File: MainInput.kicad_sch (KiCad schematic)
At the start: 26 parts, among them J14 PJ-082BH, J15 DB9_Female_RA, J33 Conn_01x04_Female, U9 MAX3232

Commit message: First try to fit electronic on PCB
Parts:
- removed TP255, TP256, TP257, TP258, TP259, TP260: TestPoint_Small, Connector_PinHeader_2.54mm:PinHeader_1x01_P2.54mm_Vertical, symbol Connector:TestPoint_Small
- TP92: renamed from TP182; footprint Connector_PinHeader_2.54mm:PinHeader_1x01_P2.54mm_Vertical -> Connector_Pin:Pin_D1.0mm_L10.0mm
- TP94: renamed from TP183; footprint Connector_Pin:Pin_D1.2mm_L11.3mm_W3.0mm_Flat -> Connector_Pin:Pin_D1.0mm_L10.0mm
- TP97: renamed from TP185; footprint Connector_Pin:Pin_D1.2mm_L11.3mm_W3.0mm_Flat -> Connector_Pin:Pin_D1.0mm_L10.0mm
- TP98: renamed from TP186; footprint Connector_Pin:Pin_D1.2mm_L11.3mm_W3.0mm_Flat -> Connector_Pin:Pin_D1.0mm_L10.0mm
- renumbered D48 to D34, D49 to D35, J14 to J27, J15 to J28, J33 to J29, NT456 to NT468, NT457 to NT469, R81 to R68

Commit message: backup 1 bank done
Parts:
- NT468, NT469: footprint NetTie:NetTie-2_THT_Pad1.0mm -> NetTie:NetTie-2_Front1.0mm
- TP92, TP94, TP97, TP98: footprint Connector_Pin:Pin_D1.0mm_L10.0mm -> Connector_Pin:Pin_D0.9mm_L10.0mm_W2.4mm_FlatFork
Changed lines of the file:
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@@
       (effects (font (size 1.27 1.27)) (justify left))
     )
-    (property "Footprint" "Connector_Pin:Pin_D1.0mm_L10.0mm" (id 2) (at 105.41 107.95 0)
+    (property "Footprint" "Connector_Pin:Pin_D0.9mm_L10.0mm_W2.4mm_FlatFork" (id 2) (at 105.41 107.95 0)
       (effects (font (size 1.27 1.27)) hide)
     )
@@
       (effects (font (size 1.27 1.27)) (justify left))
     )
-    (property "Footprint" "Connector_Pin:Pin_D1.0mm_L10.0mm" (id 2) (at 63.5 102.87 0)
+    (property "Footprint" "Connector_Pin:Pin_D0.9mm_L10.0mm_W2.4mm_FlatFork" (id 2) (at 63.5 102.87 0)
       (effects (font (size 1.27 1.27)) hide)
     )
@@
     (property "Reference" "NT469" (id 0) (at 110.49 106.68 0))
     (property "Value" "SER_11" (id 1) (at 110.49 109.22 0))
-    (property "Footprint" "NetTie:NetTie-2_THT_Pad1.0mm" (id 2) (at 110.49 107.95 0)
+    (property "Footprint" "NetTie:NetTie-2_Front1.0mm" (id 2) (at 110.49 107.95 0)
       (effects (font (size 1.27 1.27)) hide)
     )
@@
     (property "Reference" "NT468" (id 0) (at 109.22 96.52 0))
     (property "Value" "SER_12" (id 1) (at 109.22 99.06 0))
-    (property "Footprint" "NetTie:NetTie-2_THT_Pad1.0mm" (id 2) (at 109.22 97.79 0)
+    (property "Footprint" "NetTie:NetTie-2_Front1.0mm" (id 2) (at 109.22 97.79 0)
       (effects (font (size 1.27 1.27)) hide)
     )
@@
       (effects (font (size 1.27 1.27)) (justify left))
     )
-    (property "Footprint" "Connector_Pin:Pin_D1.0mm_L10.0mm" (id 2) (at 63.5 107.95 0)
+    (property "Footprint" "Connector_Pin:Pin_D0.9mm_L10.0mm_W2.4mm_FlatFork" (id 2) (at 63.5 107.95 0)
       (effects (font (size 1.27 1.27)) hide)
     )
@@
       (effects (font (size 1.27 1.27)) (justify left))
     )
-    (property "Footprint" "Connector_Pin:Pin_D1.0mm_L10.0mm" (id 2) (at 105.41 97.79 0)
-      (effects (font (size 1.27 1.27)) hide)
-    )
+    (property "Footprint" "Connector_Pin:Pin_D0.9mm_L10.0mm_W2.4mm_FlatFork" (id 2) (at 105.41 97.79 0)
+      (effects (font (size 1.27 1.27)) hide)
+    )

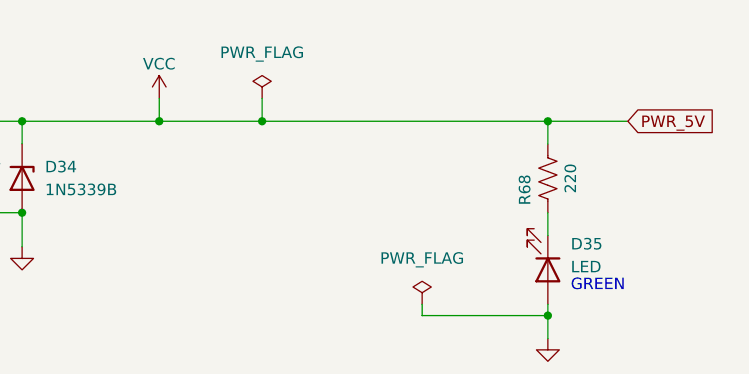
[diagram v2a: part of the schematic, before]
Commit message: half PCB completed
FTS io controller PCB
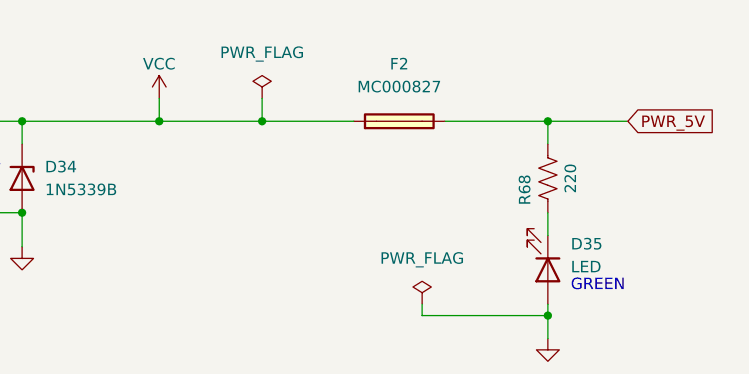
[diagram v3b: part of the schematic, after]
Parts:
- added F2: MC000827, SnapEDA Library:MC000827, symbol MC000827:MC000827
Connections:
- net VCC: now also F2.P$1; no longer R68.2
- new net PWR_5V: F2.P$2, R68.2
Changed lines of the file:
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@@
   (junction (at 116.84 77.47) (diameter 0) (color 0 0 0 0)
   )
+  (junction (at 116.84 140.97) (diameter 0) (color 0 0 0 0)
+  )
+  (junction (at 172.72 30.48) (diameter 0) (color 0 0 0 0)
+  )
+  (junction (at 123.19 107.95) (diameter 0) (color 0 0 0 0)
+  )
+  (junction (at 114.3 30.48) (diameter 0) (color 0 0 0 0)
+  )
   (junction (at 140.97 30.48) (diameter 0) (color 0 0 0 0)
   )
-  (junction (at 116.84 140.97) (diameter 0) (color 0 0 0 0)
-  )
-  (junction (at 123.19 107.95) (diameter 0) (color 0 0 0 0)
-  )
-  (junction (at 114.3 30.48) (diameter 0) (color 0 0 0 0)
-  )
-  (junction (at 172.72 30.48) (diameter 0) (color 0 0 0 0)
-  )
   (junction (at 120.65 140.97) (diameter 0) (color 0 0 0 0)
   )
@@
     (stroke (width 0) (type default) (color 0 0 0 0))
   )
+  (wire (pts (xy 161.29 30.48) (xy 172.72 30.48))
+    (stroke (width 0) (type default) (color 0 0 0 0))
+  )
   (polyline (pts (xy 24.13 158.75) (xy 130.81 158.75))
     (stroke (width 0) (type default) (color 0 0 0 0))
@@
     (stroke (width 0) (type default) (color 0 0 0 0))
   )
-  (wire (pts (xy 140.97 30.48) (xy 172.72 30.48))
+  (wire (pts (xy 140.97 30.48) (xy 151.13 30.48))
     (stroke (width 0) (type default) (color 0 0 0 0))
   )
@@
     (pin "2")
   )
+  (symbol (lib_id "MC000827:MC000827") (at 156.21 30.48 0) (unit 1)
+    (in_bom yes) (on_board yes) (fields_autoplaced)
+    (property "Reference" "F2" (id 0) (at 156.21 24.13 0))
+    (property "Value" "MC000827" (id 1) (at 156.21 26.67 0))
+    (property "Footprint" "SnapEDA Library:MC000827" (id 2) (at 156.21 30.48 0)
+      (effects (font (size 1.27 1.27)) (justify left bottom) hide)
+    )
+    (property "Datasheet" "" (id 3) (at 156.21 30.48 0)
+      (effects (font (size 1.27 1.27)) (justify left bottom) hide)
+    )
+    (pin "P$1")
+    (pin "P$2")
+  )
   (symbol (lib_id "Connector:TestPoint") (at 63.5 97.79 90) (mirror x) (unit 1)

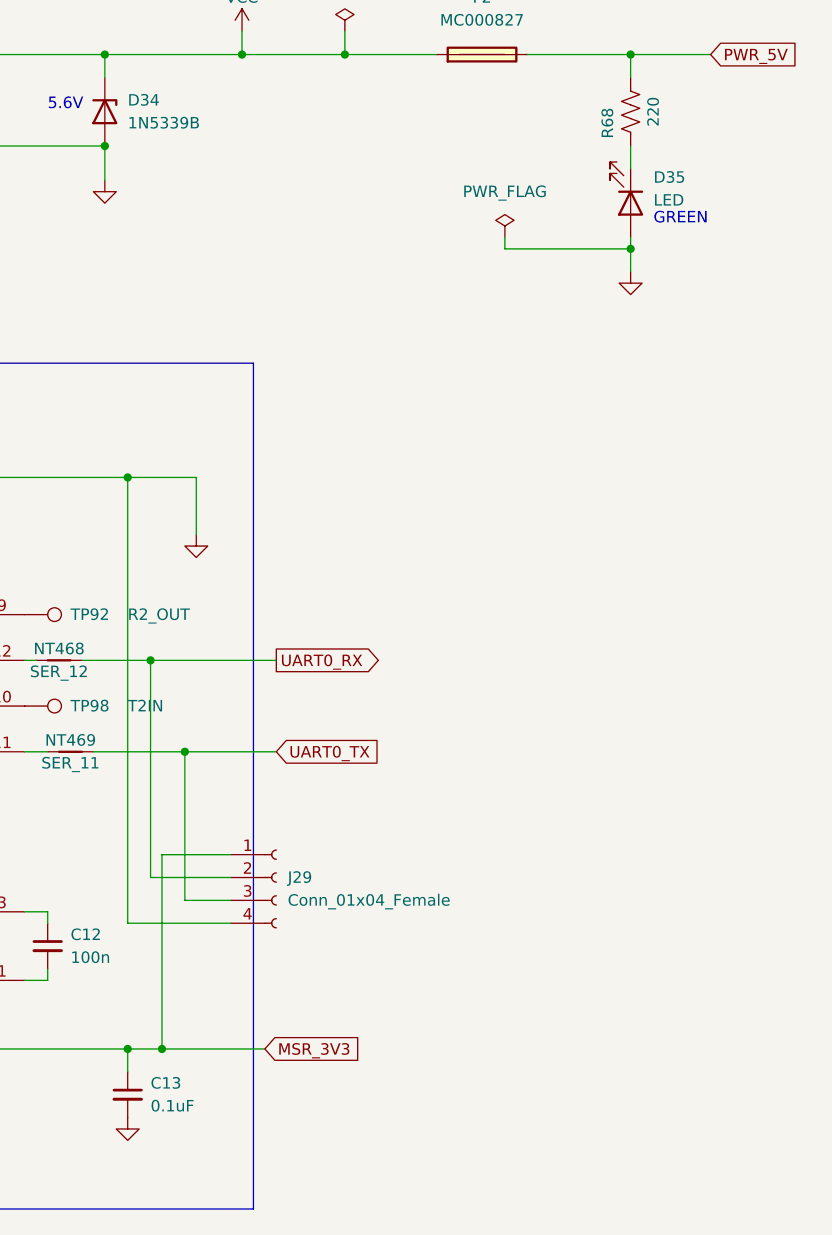
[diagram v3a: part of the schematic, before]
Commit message: PCB Completed
PCB completed but final verification not completed
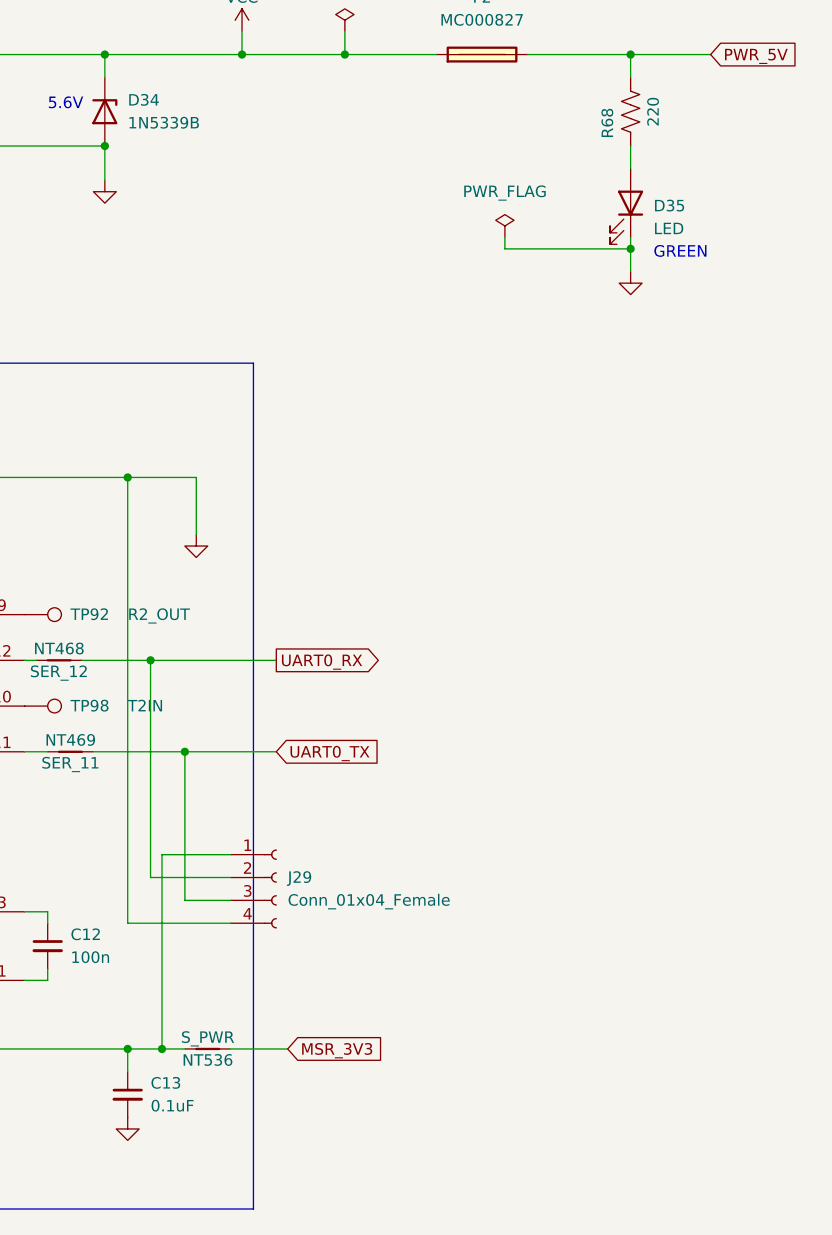
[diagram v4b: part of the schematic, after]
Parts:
- added NT536: S_PWR, NetTie:NetTie-2_Front1.0mm, symbol Device:NetTie_2
- J29: footprint Connector_PinHeader_2.54mm:PinHeader_1x04_P2.54mm_Vertical -> Connector_PinSocket_2.54mm:PinSocket_1x04_P2.54mm_Vertical
- TP92, TP94, TP97, TP98: footprint Connector_Pin:Pin_D0.9mm_L10.0mm_W2.4mm_FlatFork -> TestPoint:TestPoint_THTPad_D1.5mm_Drill0.7mm
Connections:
- net GND: now also D35.1 (K); no longer D35.2 (A)
- net MSR_3V3: now also NT536.1; no longer C13.1, J29.1 (Pin_1), U9.16 (VCC)
- net at R68.1: now also D35.2 (A); no longer D35.1 (K)
- new net: C13.1, J29.1 (Pin_1), NT536.2, U9.16 (VCC)
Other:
- moved on the sheet: D35
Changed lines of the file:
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@@
   (junction (at 172.72 30.48) (diameter 0) (color 0 0 0 0)
   )
+  (junction (at 120.65 140.97) (diameter 0) (color 0 0 0 0)
+  )
   (junction (at 123.19 107.95) (diameter 0) (color 0 0 0 0)
   )
@@
   (junction (at 140.97 30.48) (diameter 0) (color 0 0 0 0)
   )
-  (junction (at 120.65 140.97) (diameter 0) (color 0 0 0 0)
-  )
   (junction (at 172.72 52.07) (diameter 0) (color 0 0 0 0)
   )
@@
     (stroke (width 0) (type default) (color 0 0 0 0))
   )
+  (wire (pts (xy 128.27 140.97) (xy 134.62 140.97))
+    (stroke (width 0) (type default) (color 0 0 0 0))
+  )
   (wire (pts (xy 52.07 90.17) (xy 39.37 90.17))
     (stroke (width 0) (type default) (color 0 0 0 0))
@@
     (stroke (width 0) (type default) (color 0 0 0 0))
   )
+  (wire (pts (xy 120.65 140.97) (xy 123.19 140.97))
+    (stroke (width 0) (type default) (color 0 0 0 0))
+  )
   (wire (pts (xy 158.75 52.07) (xy 172.72 52.07))
     (stroke (width 0) (type default) (color 0 0 0 0))
@@
   )
   (wire (pts (xy 64.77 107.95) (xy 52.07 107.95))
-    (stroke (width 0) (type default) (color 0 0 0 0))
-  )
-  (wire (pts (xy 120.65 140.97) (xy 132.08 140.97))
     (stroke (width 0) (type default) (color 0 0 0 0))
   )
@@
     (effects (font (size 1.27 1.27)) (justify left bottom))
   )
-  (text "GREEN" (at 175.26 49.53 0)
+  (text "GREEN" (at 175.26 53.34 0)
     (effects (font (size 1.27 1.27)) (justify left bottom))
   )
@@
     )
   )
-  (global_label "MSR_3V3" (shape input) (at 132.08 140.97 0) (fields_autoplaced)
+  (global_label "MSR_3V3" (shape input) (at 134.62 140.97 0) (fields_autoplaced)
     (effects (font (size 1.27 1.27)) (justify left))
-    (property "Intersheet References" "${INTERSHEET_REFS}" (id 0) (at 142.8993 140.8906 0)
+    (property "Intersheet References" "${INTERSHEET_REFS}" (id 0) (at 145.4393 140.8906 0)
       (effects (font (size 1.27 1.27)) (justify left) hide)
     )
@@
       (effects (font (size 1.27 1.27)) (justify left))
     )
-    (property "Footprint" "Connector_Pin:Pin_D0.9mm_L10.0mm_W2.4mm_FlatFork" (id 2) (at 105.41 107.95 0)
+    (property "Footprint" "TestPoint:TestPoint_THTPad_D1.5mm_Drill0.7mm" (id 2) (at 105.41 107.95 0)
       (effects (font (size 1.27 1.27)) hide)
     )
@@
       (effects (font (size 1.27 1.27)) (justify left))
     )
-    (property "Footprint" "Connector_Pin:Pin_D0.9mm_L10.0mm_W2.4mm_FlatFork" (id 2) (at 63.5 102.87 0)
+    (property "Footprint" "TestPoint:TestPoint_THTPad_D1.5mm_Drill0.7mm" (id 2) (at 63.5 102.87 0)
       (effects (font (size 1.27 1.27)) hide)
     )
@@
       (effects (font (size 1.27 1.27)) (justify left))
     )
-    (property "Footprint" "Connector_PinHeader_2.54mm:PinHeader_1x04_P2.54mm_Vertical" (id 2) (at 133.35 121.92 0)
+    (property "Footprint" "Connector_PinSocket_2.54mm:PinSocket_1x04_P2.54mm_Vertical" (id 2) (at 133.35 121.92 0)
       (effects (font (size 1.27 1.27)) hide)
     )
@@
     )
     (pin "1")
+  )
+  (symbol (lib_id "Device:NetTie_2") (at 125.73 140.97 180) (unit 1)
+    (in_bom yes) (on_board yes)
+    (property "Reference" "NT536" (id 0) (at 125.73 142.24 0))
+    (property "Value" "S_PWR" (id 1) (at 125.73 139.7 0))
+    (property "Footprint" "NetTie:NetTie-2_Front1.0mm" (id 2) (at 125.73 140.97 0)
+      (effects (font (size 1.27 1.27)) hide)
+    )
+    (property "Datasheet" "~" (id 3) (at 125.73 140.97 0)
+      (effects (font (size 1.27 1.27)) hide)
+    )
+    (pin "1")
+    (pin "2")
   )
   (symbol (lib_id "Device:C_Small") (at 107.95 129.54 0) (unit 1)
@@
     (pin "4")
   )
-  (symbol (lib_id "Device:LED") (at 172.72 46.99 270) (unit 1)
-    (in_bom yes) (on_board yes) (fields_autoplaced)
-    (property "Reference" "D35" (id 0) (at 175.26 44.1324 90)
-      (effects (font (size 1.27 1.27)) (justify left))
-    )
-    (property "Value" "LED" (id 1) (at 175.26 46.6724 90)
+  (symbol (lib_id "Device:LED") (at 172.72 46.99 270) (mirror x) (unit 1)
+    (in_bom yes) (on_board yes) (fields_autoplaced)
+    (property "Reference" "D35" (id 0) (at 175.26 47.3074 90)
+      (effects (font (size 1.27 1.27)) (justify left))
+    )
+    (property "Value" "LED" (id 1) (at 175.26 49.8474 90)
       (effects (font (size 1.27 1.27)) (justify left))
     )
@@
       (effects (font (size 1.27 1.27)) (justify left))
     )
-    (property "Footprint" "Connector_Pin:Pin_D0.9mm_L10.0mm_W2.4mm_FlatFork" (id 2) (at 63.5 107.95 0)
+    (property "Footprint" "TestPoint:TestPoint_THTPad_D1.5mm_Drill0.7mm" (id 2) (at 63.5 107.95 0)
       (effects (font (size 1.27 1.27)) hide)
     )
@@
       (effects (font (size 1.27 1.27)) (justify left))
     )
-    (property "Footprint" "Connector_Pin:Pin_D0.9mm_L10.0mm_W2.4mm_FlatFork" (id 2) (at 105.41 97.79 0)
-      (effects (font (size 1.27 1.27)) hide)
-    )
+    (property "Footprint" "TestPoint:TestPoint_THTPad_D1.5mm_Drill0.7mm" (id 2) (at 105.41 97.79 0)
+      (effects (font (size 1.27 1.27)) hide)
+    )

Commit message: small update silkscreen
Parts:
- added TP84: RTS, TestPoint:TestPoint_THTPad_D1.5mm_Drill0.7mm, symbol Connector:TestPoint
- added TP85: CTS, TestPoint:TestPoint_THTPad_D1.5mm_Drill0.7mm, symbol Connector:TestPoint
- C10, C11, C12, C9: footprint Capacitor_SMD:C_0201_0603Metric_Pad0.64x0.40mm_HandSolder -> Capacitor_SMD:C_0603_1608Metric_Pad1.08x0.95mm_HandSolder
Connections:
- net RXD: now reaches J28.2, U9.14 (T1OUT)
- net TXD: now reaches J28.3, U9.8 (R2IN)
- net at J28.7: now also TP84.1
- net at J28.8: now also TP85.1
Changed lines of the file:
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@@
     (stroke (width 0) (type default) (color 0 0 0 0))
   )
-  (wire (pts (xy 52.07 90.17) (xy 39.37 90.17))
+  (wire (pts (xy 58.42 90.17) (xy 39.37 90.17))
     (stroke (width 0) (type default) (color 0 0 0 0))
   )
@@
     (stroke (width 0) (type default) (color 0 0 0 0))
   )
-  (wire (pts (xy 64.77 107.95) (xy 52.07 107.95))
+  (wire (pts (xy 64.77 107.95) (xy 58.42 107.95))
     (stroke (width 0) (type default) (color 0 0 0 0))
   )
@@
     (stroke (width 0) (type default) (color 0 0 0 0))
   )
-  (wire (pts (xy 52.07 107.95) (xy 52.07 90.17))
+  (wire (pts (xy 58.42 107.95) (xy 58.42 90.17))
     (stroke (width 0) (type default) (color 0 0 0 0))
   )
@@
     (effects (font (size 1.27 1.27)) (justify left bottom))
   )
+  (label "TXD" (at 49.53 95.25 0)
+    (effects (font (size 1.27 1.27)) (justify left bottom))
+  )
+  (label "RXD" (at 49.53 90.17 0)
+    (effects (font (size 1.27 1.27)) (justify left bottom))
+  )
   (global_label "PWR_5V" (shape input) (at 181.61 30.48 0) (fields_autoplaced)
     (effects (font (size 1.27 1.27)) (justify left))
@@
       (effects (font (size 1.27 1.27)) (justify left))
     )
-    (property "Footprint" "Capacitor_SMD:C_0201_0603Metric_Pad0.64x0.40mm_HandSolder" (id 2) (at 58.42 129.54 0)
+    (property "Footprint" "Capacitor_SMD:C_0603_1608Metric_Pad1.08x0.95mm_HandSolder" (id 2) (at 58.42 129.54 0)
       (effects (font (size 1.27 1.27)) hide)
     )
@@
     )
     (property "Datasheet" "" (id 3) (at 172.72 54.61 0)
+      (effects (font (size 1.27 1.27)) hide)
+    )
+    (pin "1")
+  )
+  (symbol (lib_id "Connector:TestPoint") (at 39.37 92.71 270) (unit 1)
+    (in_bom yes) (on_board yes)
+    (property "Reference" "TP84" (id 0) (at 44.45 92.71 90)
+      (effects (font (size 1.27 1.27)) (justify left))
+    )
+    (property "Value" "RTS" (id 1) (at 49.53 92.71 90)
+      (effects (font (size 1.27 1.27)) (justify left))
+    )
+    (property "Footprint" "TestPoint:TestPoint_THTPad_D1.5mm_Drill0.7mm" (id 2) (at 39.37 97.79 0)
+      (effects (font (size 1.27 1.27)) hide)
+    )
+    (property "Datasheet" "~" (id 3) (at 39.37 97.79 0)
       (effects (font (size 1.27 1.27)) hide)
     )
@@
       (effects (font (size 1.27 1.27)) (justify left))
     )
-    (property "Footprint" "Capacitor_SMD:C_0201_0603Metric_Pad0.64x0.40mm_HandSolder" (id 2) (at 48.26 128.27 0)
+    (property "Footprint" "Capacitor_SMD:C_0603_1608Metric_Pad1.08x0.95mm_HandSolder" (id 2) (at 48.26 128.27 0)
       (effects (font (size 1.27 1.27)) hide)
     )
@@
     (pin "1")
     (pin "2")
+  )
+  (symbol (lib_id "Connector:TestPoint") (at 39.37 97.79 270) (unit 1)
+    (in_bom yes) (on_board yes)
+    (property "Reference" "TP85" (id 0) (at 44.45 97.79 90)
+      (effects (font (size 1.27 1.27)) (justify left))
+    )
+    (property "Value" "CTS" (id 1) (at 49.53 97.79 90)
+      (effects (font (size 1.27 1.27)) (justify left))
+    )
+    (property "Footprint" "TestPoint:TestPoint_THTPad_D1.5mm_Drill0.7mm" (id 2) (at 39.37 102.87 0)
+      (effects (font (size 1.27 1.27)) hide)
+    )
+    (property "Datasheet" "~" (id 3) (at 39.37 102.87 0)
+      (effects (font (size 1.27 1.27)) hide)
+    )
+    (pin "1")
   )
   (symbol (lib_id "power:GND") (at 39.37 107.95 0) (unit 1)
@@
       (effects (font (size 1.27 1.27)) (justify left))
     )
-    (property "Footprint" "Capacitor_SMD:C_0201_0603Metric_Pad0.64x0.40mm_HandSolder" (id 2) (at 107.95 129.54 0)
+    (property "Footprint" "Capacitor_SMD:C_0603_1608Metric_Pad1.08x0.95mm_HandSolder" (id 2) (at 107.95 129.54 0)
       (effects (font (size 1.27 1.27)) hide)
     )
@@
       (effects (font (size 1.27 1.27)) (justify left))
     )
-    (property "Footprint" "Capacitor_SMD:C_0201_0603Metric_Pad0.64x0.40mm_HandSolder" (id 2) (at 39.37 128.27 0)
-      (effects (font (size 1.27 1.27)) hide)
-    )
+    (property "Footprint" "Capacitor_SMD:C_0603_1608Metric_Pad1.08x0.95mm_HandSolder" (id 2) (at 39.37 128.27 0)
+      (effects (font (size 1.27 1.27)) hide)
+    )

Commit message: update
Correction of small error
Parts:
- removed NT536: S_PWR, NetTie:NetTie-2_Front1.0mm, symbol Device:NetTie_2
- added J34: Conn_01x04_Female, Connector_PinSocket_2.54mm:PinSocket_1x04_P2.54mm_Vertical, symbol Connector:Conn_01x04_Female
- added J35: Conn_01x03_Male, Connector_PinSocket_2.54mm:PinSocket_1x03_P2.54mm_Vertical, symbol Connector:Conn_01x03_Male
- added Q4: NPD6020P, Package_TO_SOT_THT:TO-220-3_Horizontal_TabDown, symbol Transistor_FET:BSS84
- added Q5: 2N2222, Package_TO_SOT_THT:TO-92_Inline, symbol Transistor_BJT:2N3904
- added R6: 220, Resistor_THT:R_Axial_DIN0207_L6.3mm_D2.5mm_P10.16mm_Horizontal, symbol Device:R_US
- added R7: 10K, Resistor_THT:R_Axial_DIN0207_L6.3mm_D2.5mm_P10.16mm_Horizontal, symbol Device:R_US
- R68: footprint Resistor_THT:R_Axial_DIN0309_L9.0mm_D3.2mm_P12.70mm_Horizontal -> Resistor_THT:R_Axial_DIN0207_L6.3mm_D2.5mm_P10.16mm_Horizontal
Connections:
- net GND: now also J34.1 (Pin_1), Q5.1 (E)
- net MSR_3V3: now also J35.3 (Pin_3)
- net UART0_RX: now also J34.3 (Pin_3)
- net UART0_TX: now also J34.2 (Pin_2)
- net VCC: now also J35.1 (Pin_1), Q4.2 (S), R6.2; no longer F2.P$1
- net SVCC: now reaches C13.1, J29.1 (Pin_1), U9.16 (VCC)
- net SVCC: now also J34.4 (Pin_4), J35.2 (Pin_2)
- new net: Q4.1 (G), Q5.3 (C), R6.1
- new net: F2.P$1, Q4.3 (D)
- new net: Q5.2 (B), R7.1
- new net OE: R7.2
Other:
- note added: "2 CONNECTORS ARE AVAILABLE TO ACCEPT ANY SERIAL MODULE"
- note added: "FOOTPRINT WILL ACCEPT DIRECT IC SOLDERING OR PIGGY BACK MODULE MOUNTED IN REVERSE ON 4 PINS CONNECTOR OR STRAIGHT WITH 4 WIRES CABLE"
- note added: "G700P06J G050P03T"
- note added: "IRLU3410PBF RFP15N05L SFT1342"
- note added: "NPD6020P"
- note added: "NTD20N06L"
- note added: "SERIAL MODULE POWER IS SELECTABLE BETWEEN 3.3V AND 5V. SOME SERIAL MODULE WORK ONLY AT 5V"
- note removed: "FOOTPRINT WILL ACCEPT DIRECT IC SOLDERING OR PIGGY BACK MODULE MOUNTED ON TP"
- moved on the sheet: D35, F2, J29, R68
